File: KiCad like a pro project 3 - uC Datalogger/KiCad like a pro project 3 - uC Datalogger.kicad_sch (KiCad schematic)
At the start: 0 parts

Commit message: components placed
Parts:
- added BT?: Battery, symbol Device:Battery
- added C? (x4): C, symbol Device:C
- added C?: C_Polarized, symbol Device:C_Polarized
- added D? (x2): LED, symbol Device:LED
- added H? (x4): MountingHole, symbol Mechanical:MountingHole
- added R? (x7): R, symbol Device:R
- added U?: DS1337S+, SOIC127P600X175-8N, symbol DS1337S_:DS1337S+
- added U? (x2): 24LC1025, symbol Memory_EEPROM:24LC1025
- added U?: ATMEGA328P_VQFNVQFN, VQFN-28, symbol SparkFun-IC-Microcontroller:ATMEGA328P_VQFNVQFN
- added Y? (x2): Crystal, symbol Device:Crystal
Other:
- added sheet Connectors (Connectors.kicad_sch)

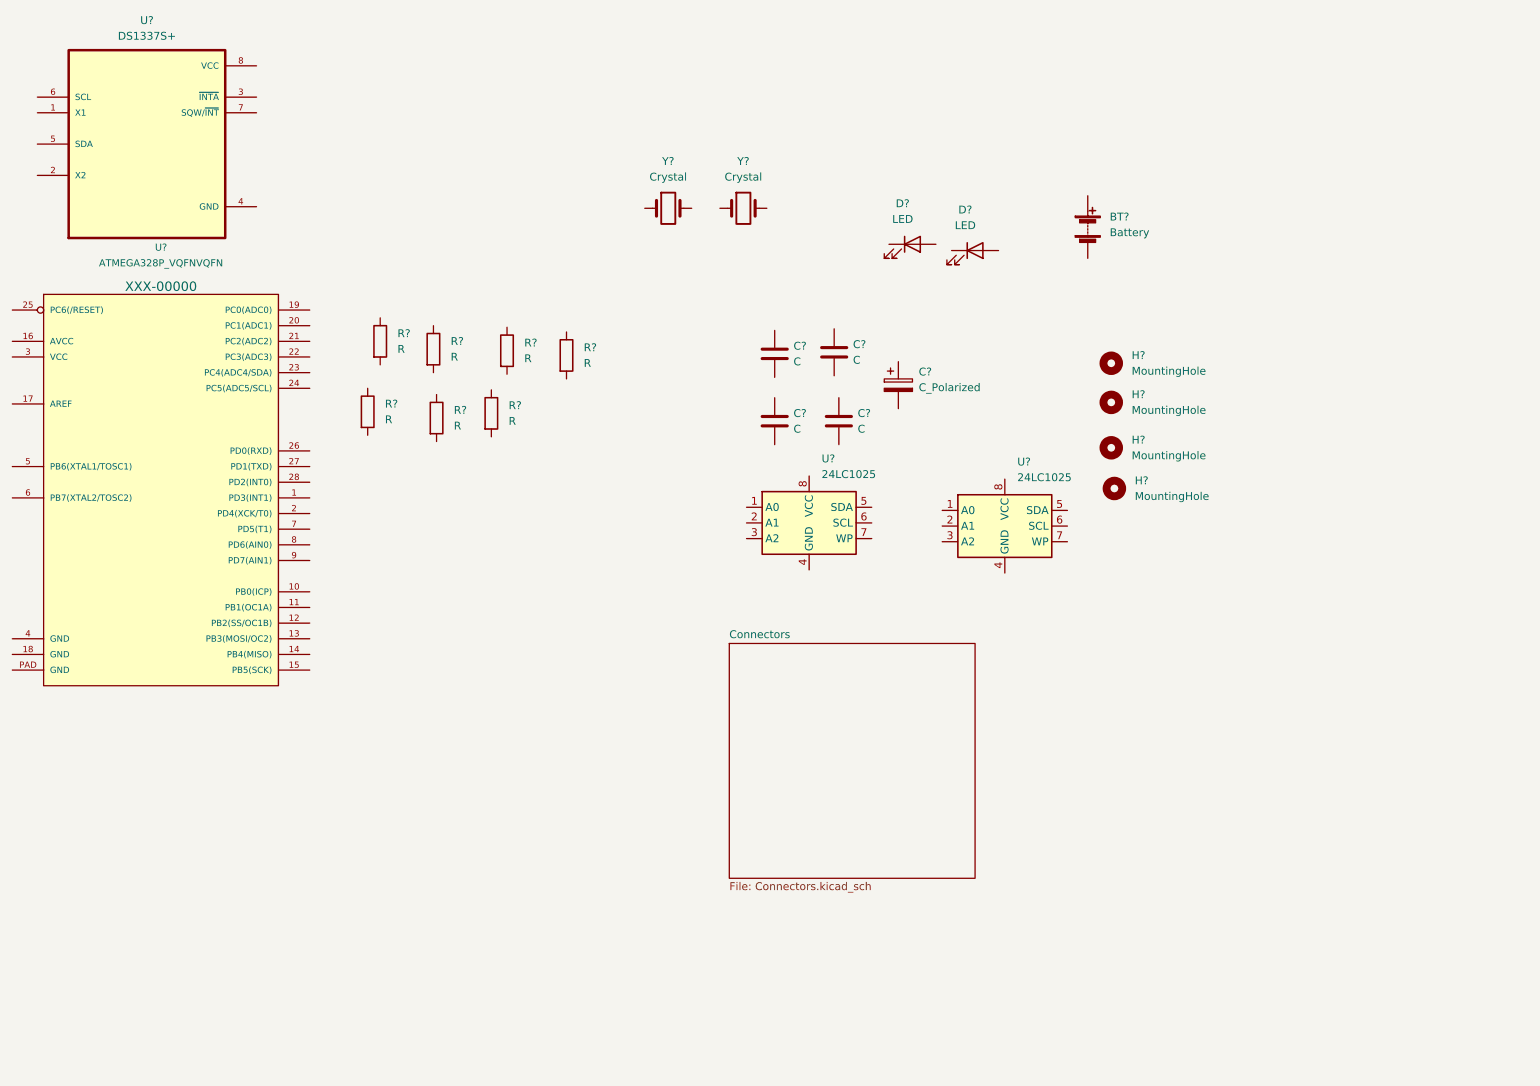
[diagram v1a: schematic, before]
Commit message: changed locations of symbols (arrange)
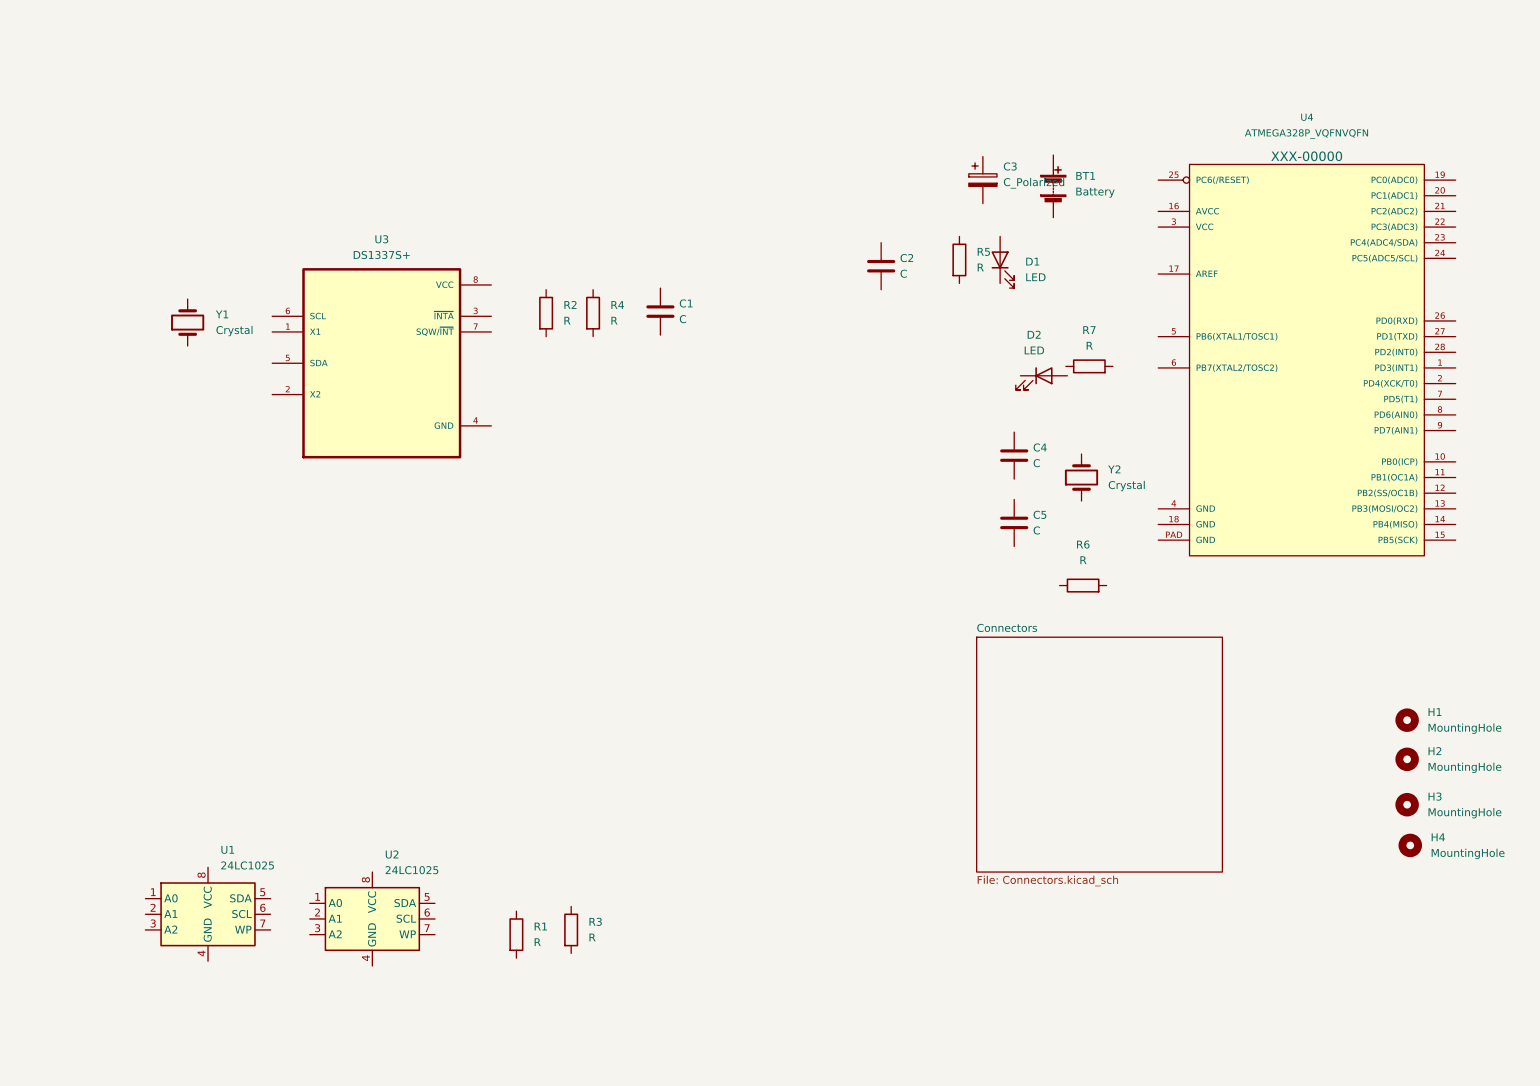
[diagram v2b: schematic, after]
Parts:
- gave numbers to parts that had none: 25
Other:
- moved on the sheet: BT1, C1, C2, C3, C4, C5, D1, D2, H1, H2, H3, H4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

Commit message: added component values
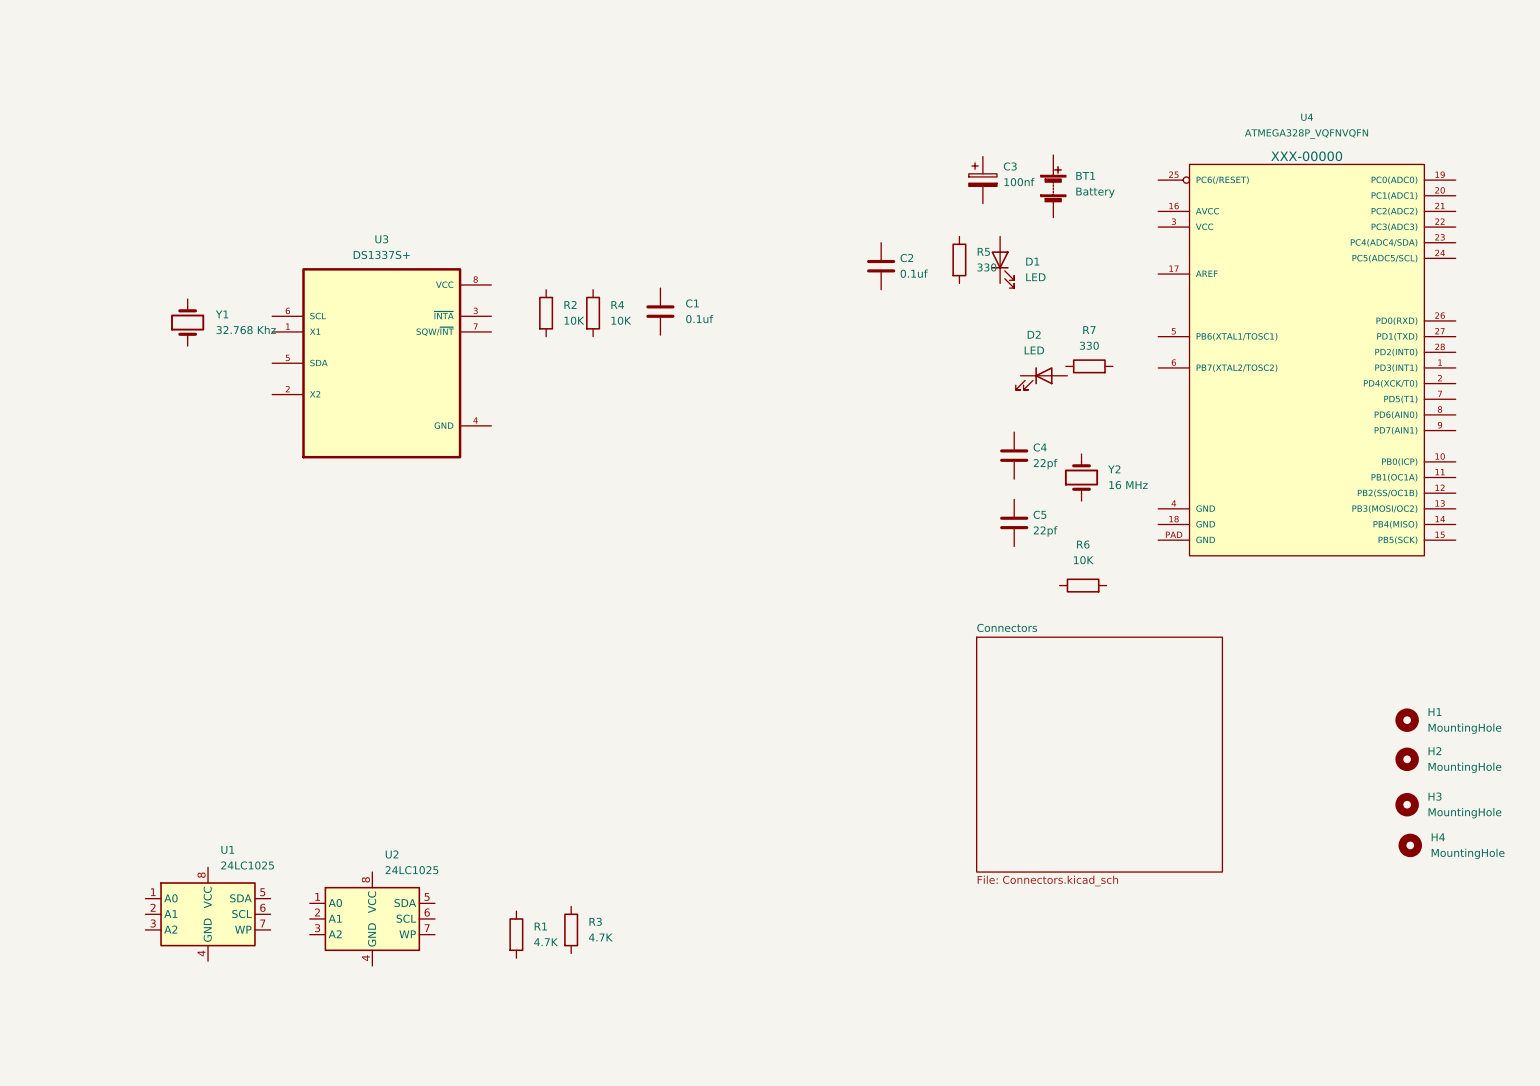
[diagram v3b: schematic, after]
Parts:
- C1, C2: value C -> 0.1uf
- C3: value C_Polarized -> 100nf
- C4, C5: value C -> 22pf
- R1, R3: value R -> 4.7K
- R2, R4, R6: value R -> 10K
- R5, R7: value R -> 330
- Y1: value Crystal -> 32.768 Khz
- Y2: value Crystal -> 16 MHz
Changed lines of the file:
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@@
       (effects (font (size 1.27 1.27)) (justify left))
     )
-    (property "Value" "C" (id 1) (at 185.928 103.1239 0)
+    (property "Value" "22pf" (id 1) (at 185.928 103.1239 0)
       (effects (font (size 1.27 1.27)) (justify left))
     )
@@
     (in_bom yes) (on_board yes) (fields_autoplaced)
     (property "Reference" "R6" (id 0) (at 194.056 105.41 90))
-    (property "Value" "R" (id 1) (at 194.056 107.95 90))
+    (property "Value" "10K" (id 1) (at 194.056 107.95 90))
     (property "Footprint" "" (id 2) (at 194.056 113.792 90)
       (effects (font (size 1.27 1.27)) hide)
@@
       (effects (font (size 1.27 1.27)) (justify left))
     )
-    (property "Value" "C_Polarized" (id 1) (at 181.102 46.6089 0)
+    (property "Value" "100nf" (id 1) (at 181.102 46.6089 0)
       (effects (font (size 1.27 1.27)) (justify left))
     )
@@
       (effects (font (size 1.27 1.27)) (justify right))
     )
-    (property "Value" "Crystal" (id 1) (at 53.34 70.6119 90)
+    (property "Value" "32.768 Khz" (id 1) (at 53.34 70.6119 90)
       (effects (font (size 1.27 1.27)) (justify right))
     )
@@
       (effects (font (size 1.27 1.27)) (justify left))
     )
-    (property "Value" "R" (id 1) (at 117.348 69.0879 0)
+    (property "Value" "10K" (id 1) (at 117.348 69.0879 0)
       (effects (font (size 1.27 1.27)) (justify left))
     )
@@
     (in_bom yes) (on_board yes) (fields_autoplaced)
     (property "Reference" "R7" (id 0) (at 195.072 70.612 90))
-    (property "Value" "R" (id 1) (at 195.072 73.152 90))
+    (property "Value" "330" (id 1) (at 195.072 73.152 90))
     (property "Footprint" "" (id 2) (at 195.072 78.232 90)
       (effects (font (size 1.27 1.27)) hide)
@@
       (effects (font (size 1.27 1.27)) (justify left))
     )
-    (property "Value" "R" (id 1) (at 113.792 169.1639 0)
+    (property "Value" "4.7K" (id 1) (at 113.792 169.1639 0)
       (effects (font (size 1.27 1.27)) (justify left))
     )
@@
       (effects (font (size 1.27 1.27)) (justify left))
     )
-    (property "Value" "R" (id 1) (at 104.902 169.9259 0)
+    (property "Value" "4.7K" (id 1) (at 104.902 169.9259 0)
       (effects (font (size 1.27 1.27)) (justify left))
     )
@@
   (symbol (lib_id "Device:C") (at 125.476 67.564 0) (unit 1)
     (in_bom yes) (on_board yes) (fields_autoplaced)
-    (property "Reference" "C1" (id 0) (at 128.524 66.2939 0)
-      (effects (font (size 1.27 1.27)) (justify left))
-    )
-    (property "Value" "C" (id 1) (at 128.524 68.8339 0)
+    (property "Reference" "C1" (id 0) (at 129.54 66.2939 0)
+      (effects (font (size 1.27 1.27)) (justify left))
+    )
+    (property "Value" "0.1uf" (id 1) (at 129.54 68.8339 0)
       (effects (font (size 1.27 1.27)) (justify left))
     )
@@
       (effects (font (size 1.27 1.27)) (justify left))
     )
-    (property "Value" "C" (id 1) (at 164.338 61.4679 0)
+    (property "Value" "0.1uf" (id 1) (at 164.338 61.4679 0)
       (effects (font (size 1.27 1.27)) (justify left))
     )
@@
       (effects (font (size 1.27 1.27)) (justify left))
     )
-    (property "Value" "R" (id 1) (at 109.728 69.0879 0)
+    (property "Value" "10K" (id 1) (at 109.728 69.0879 0)
       (effects (font (size 1.27 1.27)) (justify left))
     )
@@
       (effects (font (size 1.27 1.27)) (justify left))
     )
-    (property "Value" "C" (id 1) (at 185.928 92.2019 0)
+    (property "Value" "22pf" (id 1) (at 185.928 92.2019 0)
       (effects (font (size 1.27 1.27)) (justify left))
     )
@@
       (effects (font (size 1.27 1.27)) (justify left))
     )
-    (property "Value" "R" (id 1) (at 176.784 60.4519 0)
+    (property "Value" "330" (id 1) (at 176.784 60.4519 0)
       (effects (font (size 1.27 1.27)) (justify left))
     )
@@
       (effects (font (size 1.27 1.27)) (justify right))
     )
-    (property "Value" "Crystal" (id 1) (at 198.12 95.7579 90)
+    (property "Value" "16 MHz" (id 1) (at 198.12 95.7579 90)
       (effects (font (size 1.27 1.27)) (justify right))
     )
@@
     )
     (path "/a23a281b-3230-4190-b7b1-7479cb72f922"
-      (reference "C1") (unit 1) (value "C") (footprint "")
+      (reference "C1") (unit 1) (value "0.1uf") (footprint "")
     )
     (path "/bcea5304-0f3c-468c-836f-f44241c56e39"
-      (reference "C2") (unit 1) (value "C") (footprint "")
+      (reference "C2") (unit 1) (value "0.1uf") (footprint "")
     )
     (path "/47eb796d-6260-47b3-b1f3-fe01c6d8421d"
-      (reference "C3") (unit 1) (value "C_Polarized") (footprint "")
+      (reference "C3") (unit 1) (value "100nf") (footprint "")
     )
     (path "/e68416c6-709b-4929-b482-73ee7f731ec2"
-      (reference "C4") (unit 1) (value "C") (footprint "")
+      (reference "C4") (unit 1) (value "22pf") (footprint "")
     )
     (path "/38696296-9013-4c0b-8502-8baef73c8954"
-      (reference "C5") (unit 1) (value "C") (footprint "")
+      (reference "C5") (unit 1) (value "22pf") (footprint "")
     )
     (path "/0c13359b-dc83-4d5d-a8db-7a6718f66973"
@@
     )
     (path "/9db5fda2-df5e-494d-a223-3a30e666d007"
-      (reference "R1") (unit 1) (value "R") (footprint "")
+      (reference "R1") (unit 1) (value "4.7K") (footprint "")
     )
     (path "/d9b6de5c-6388-4cb8-b030-b74a69ad54e5"
-      (reference "R2") (unit 1) (value "R") (footprint "")
+      (reference "R2") (unit 1) (value "10K") (footprint "")
     )
     (path "/670f1c70-8fed-4569-aa2e-f3c1b6ea6186"
-      (reference "R3") (unit 1) (value "R") (footprint "")
+      (reference "R3") (unit 1) (value "4.7K") (footprint "")
     )
     (path "/50874044-cc76-4f55-98e6-3b48cb17e381"
-      (reference "R4") (unit 1) (value "R") (footprint "")
+      (reference "R4") (unit 1) (value "10K") (footprint "")
     )
     (path "/f2c9b2ff-b3ef-4683-98f5-56f001528e7c"
-      (reference "R5") (unit 1) (value "R") (footprint "")
+      (reference "R5") (unit 1) (value "330") (footprint "")
     )
     (path "/3e4f3d07-bd52-4a54-a7cf-2ccafcb35f1f"
-      (reference "R6") (unit 1) (value "R") (footprint "")
+      (reference "R6") (unit 1) (value "10K") (footprint "")
     )
     (path "/57b01107-2d1a-4cf2-8817-e1293fb92b97"
-      (reference "R7") (unit 1) (value "R") (footprint "")
+      (reference "R7") (unit 1) (value "330") (footprint "")
     )
     (path "/4cd5d58f-a4aa-4f2c-9b53-e3c1e90dbd04"
@@
     )
     (path "/4bbc67d0-a6f0-4e63-bdb4-e7c517a2a0e1"
-      (reference "Y1") (unit 1) (value "Crystal") (footprint "")
+      (reference "Y1") (unit 1) (value "32.768 Khz") (footprint "")
     )
     (path "/f2dd0c84-8536-4d5f-b72f-e66fb7b34b2a"
-      (reference "Y2") (unit 1) (value "Crystal") (footprint "")
-    )
-  )
+      (reference "Y2") (unit 1) (value "16 MHz") (footprint "")
+    )
+  )

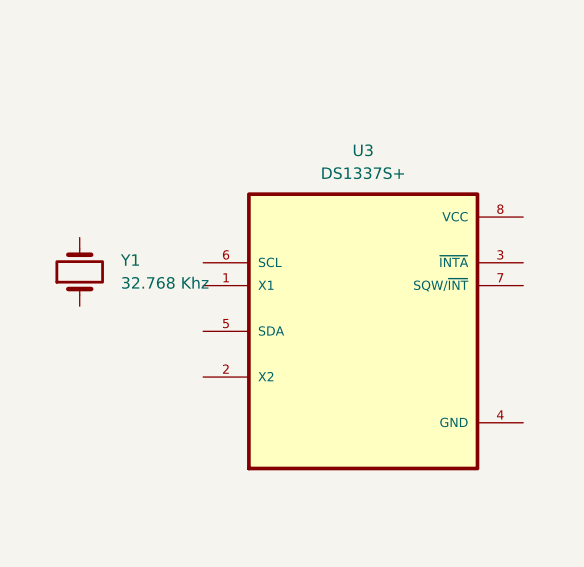
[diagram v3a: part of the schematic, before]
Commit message: completed symbol to footprint associations
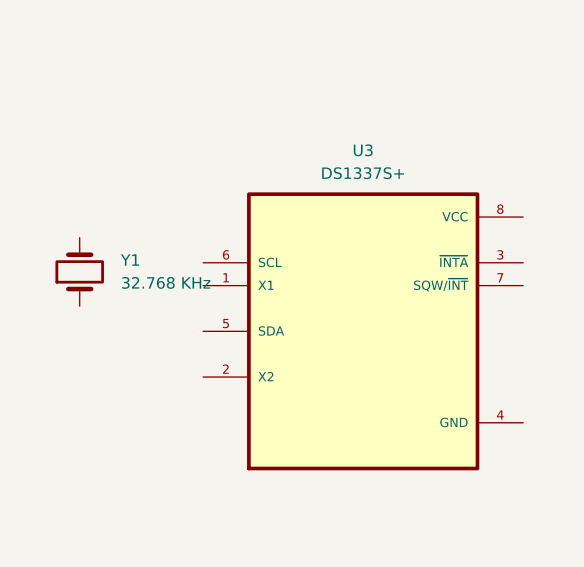
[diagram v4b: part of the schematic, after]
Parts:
- BT1: footprint (none) -> Connector_PinHeader_2.54mm:PinHeader_1x02_P2.54mm_Vertical
- C1, C2, C3, C4, C5: footprint (none) -> Capacitor_SMD:C_0805_2012Metric
- D1, D2: footprint (none) -> LED_SMD:LED_0805_2012Metric
- H1, H2, H3, H4: footprint (none) -> MountingHole:MountingHole_2.1mm
- R1, R2, R3, R4, R5, R6, R7: footprint (none) -> Resistor_SMD:R_0805_2012Metric
- U1, U2: footprint (none) -> Package_SO:SOIC-8_5.23x5.23mm_P1.27mm
- U3: footprint SOIC127P600X175-8N -> Footprints:SOIC127P600X175-8N
- U4: footprint VQFN-28 -> Footprints:QFP80P900X900X120-32N
- Y1: value 32.768 Khz -> 32.768 KHz; footprint (none) -> Crystal:Crystal_SMD_5032-2Pin_5.0x3.2mm_HandSoldering
- Y2: footprint (none) -> Crystal:Crystal_SMD_5032-2Pin_5.0x3.2mm_HandSoldering
